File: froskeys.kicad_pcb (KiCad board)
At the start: 2 copper layers, 81 x 86.3 mm, 25 parts, among them SW1 MX, SW10 RotaryEncoder_Switch, SW2 MX, SW3 MX, SW4 MX, SW5 MX, SW6 MX, SW7 MX, SW8 MX, SW9 MX, U1 XIAO-RP2040-DIP, U2 OLED

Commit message: Hi
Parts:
- moved U2 16.5 mm to (131.0, 128.7)
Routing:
- net +5V: track 0.00 -> 241.8 mm, vias 0 -> 1
- net COL3: track 0.00 -> 113.1 mm
- net ROW3: track 0.00 -> 110.5 mm
- net COL1: track 0.00 -> 105.5 mm, vias 0 -> 1
- net COL2: track 0.00 -> 103.6 mm
- net Net-(LED2-DOUT): track 0.00 -> 98.9 mm, vias 0 -> 2
- net SCL: track 0.00 -> 92.9 mm
- net SDA: track 0.00 -> 88.8 mm
- net Net-(LED1-DOUT): track 0.00 -> 78.8 mm
- net Net-(LED3-DOUT): track 0.00 -> 71.0 mm
- net Net-(D7-A): track 0.00 -> 54.1 mm
- net Net-(D4-A): track 0.00 -> 51.6 mm
- net Net-(D1-A): track 0.00 -> 46.8 mm
- net ENC_A: track 0.00 -> 41.8 mm
- net DIN: track 0.00 -> 41.4 mm
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- added copper zone on B.Cu, net GND
- added copper zone on F.Cu, net GND
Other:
- outline, holes or cut-outs redrawn
- board text added: "16.018 from top of board to top of keys"
- board text added: "Froskeys"
- board text added: "Size: 80.963 × 86.344"
- board text added: "XIAO HERE"
- board text added: "by Frosetrain"
- board text added: "{ "ViaStitching": "0.2", "stitch_zone_0": { "HSpacing": "10", "VSpacing": "10", "HOffset": "0", "VOffset": "0", "Clearance": "0", "Randomize": false } }"
- board text added: "{ "ViaStitching": "0.2", "stitch_zone_0": { "HSpacing": "10", "VSpacing": "10", "HOffset": "0", "VOffset": "0", "Clearance": "5", "Randomize": false } }"
- board text added: "{ "ViaStitching": "0.2", "stitch_zone_0": { "HSpacing": "20", "VSpacing": "20", "HOffset": "0", "VOffset": "0", "Clearance": "5", "Randomize": false } }"
- board text added: "{ "ViaStitching": "0.2", "stitch_zone_0": { "HSpacing": "5", "VSpacing": "5", "HOffset": "0", "VOffset": "0", "Clearance": "0", "Randomize": false } }"

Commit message: Seems cool
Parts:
- moved LED4 25.4 mm to (124.5, 138.4)
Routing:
- net +5V: track 241.8 -> 216.4 mm
- net Net-(LED3-DOUT): track 71.0 -> 45.8 mm
- net GND: vias 50 -> 44
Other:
- outline, holes or cut-outs redrawn

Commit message: Optimise
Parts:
- renumbered U2 to J1
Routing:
- net COL2: track 103.6 -> 102.9 mm
- net +5V: track 216.4 -> 216.9 mm
- net GND: track 1.21 -> 0.84 mm, vias 44 -> 45

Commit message: Is this good
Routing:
- net ROW3: track 110.5 -> 36.0 mm, vias 0 -> 1
- net COL3: track 113.1 -> 80.1 mm, vias 0 -> 2
- net Net-(LED2-DOUT): track 98.9 -> 84.2 mm, vias 2 -> 0
- net Net-(D1-A): track 46.8 -> 52.9 mm
- net Net-(D7-A): track 54.1 -> 49.3 mm
- net COL2: track 102.9 -> 106.3 mm
- net ROW1: track 31.0 -> 33.9 mm
- net ENC_A: track 41.8 -> 40.8 mm
- net Net-(D3-A): track 23.4 -> 24.4 mm
- net +5V: track 216.9 -> 217.3 mm, vias 1 -> 3
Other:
- board text added: "{ "ViaStitching": "0.2", "stitch_zone_0": { "HSpacing": "10", "VSpacing": "10", "HOffset": "5", "VOffset": "5", "Clearance": "0", "Randomize": false } }"

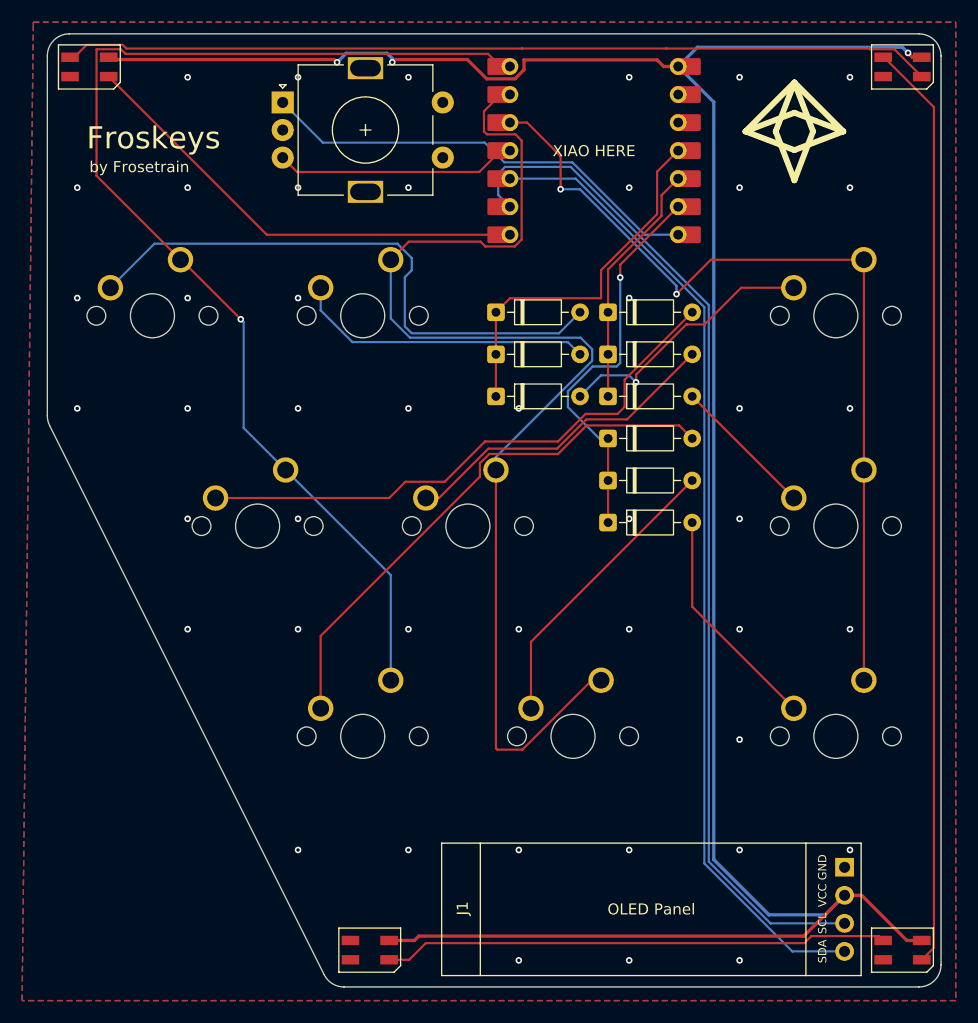
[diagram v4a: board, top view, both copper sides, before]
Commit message: Switch to SK6812MINI-E backlighting
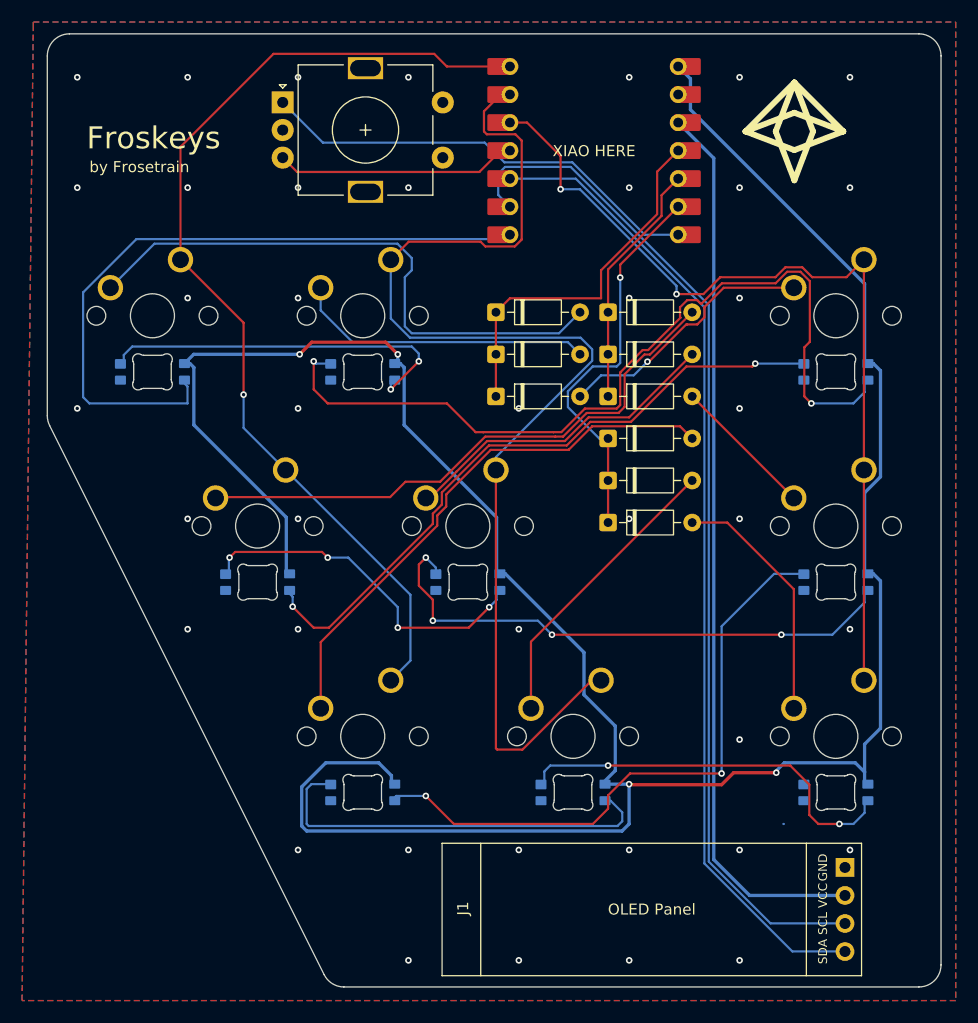
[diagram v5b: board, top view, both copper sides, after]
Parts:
- added LED5: SK6812MINI-E, Keyboard Parts:MX_SK6812MINI-E, F.Cu at (133.3, 100.0)
- added LED6: SK6812MINI-E, Keyboard Parts:MX_SK6812MINI-E, F.Cu at (166.7, 100.0)
- added LED7: SK6812MINI-E, Keyboard Parts:MX_SK6812MINI-E, F.Cu at (123.8, 119.1)
- added LED8: SK6812MINI-E, Keyboard Parts:MX_SK6812MINI-E, F.Cu at (142.9, 119.1)
- added LED9: SK6812MINI-E, Keyboard Parts:MX_SK6812MINI-E, F.Cu at (166.7, 119.1)
- LED1, LED2, LED3, LED4: value SK6812MINI -> SK6812MINI-E; footprint LED_SMD:LED_SK6812MINI_PLCC4_3.5x3.5mm_P1.75mm -> Keyboard Parts:MX_SK6812MINI-E
- moved LED3 57.8 mm to (166.7, 81.0)
- moved LED2 53.8 mm to (123.8, 81.0)
- moved LED4 39.7 mm to (114.3, 100.0)
- moved LED1 23.3 mm to (104.8, 81.0)
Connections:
- J1 pad 2: +5V -> +3V3
- LED4 pad 1: unconnected-(LED4-DOUT-Pad1) -> Net-(LED4-DOUT)
- U1 pad 12: unconnected-(U1-3V3-Pad12)_1 -> +3V3
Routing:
- net +3V3: track 0.00 -> 81.3 mm
- net Net-(LED6-DOUT): track 0.00 -> 56.8 mm, vias 0 -> 2
- net Net-(LED5-DOUT): track 0.00 -> 50.8 mm, vias 0 -> 4
- net Net-(LED1-DOUT): track 78.8 -> 33.2 mm, vias 0 -> 2
- net Net-(LED7-DOUT): track 0.00 -> 37.8 mm
- net Net-(LED8-DOUT): track 0.00 -> 35.7 mm, vias 0 -> 2
- net Net-(LED4-DOUT): track 0.00 -> 31.7 mm, vias 0 -> 4
- net +5V: track 217.3 -> 241.6 mm, vias 3 -> 4
- net DIN: track 41.4 -> 62.4 mm
- net Net-(LED3-DOUT): track 45.8 -> 60.2 mm, vias 0 -> 2
- net COL1: track 105.5 -> 91.6 mm
- net Net-(LED2-DOUT): track 84.2 -> 77.9 mm, vias 0 -> 2
- net Net-(D9-A): track 20.6 -> 22.5 mm
- net COL3: track 80.1 -> 80.8 mm
- net GND: track 0.84 -> 0.89 mm, vias 45 -> 41
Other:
- board text removed: "16.018 from top of board to top of keys"
- board text removed: "Size: 80.963 × 86.344"
